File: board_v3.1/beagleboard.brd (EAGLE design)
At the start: 69.8 x 54.6 mm, 32 parts, among them U1 DWM1000

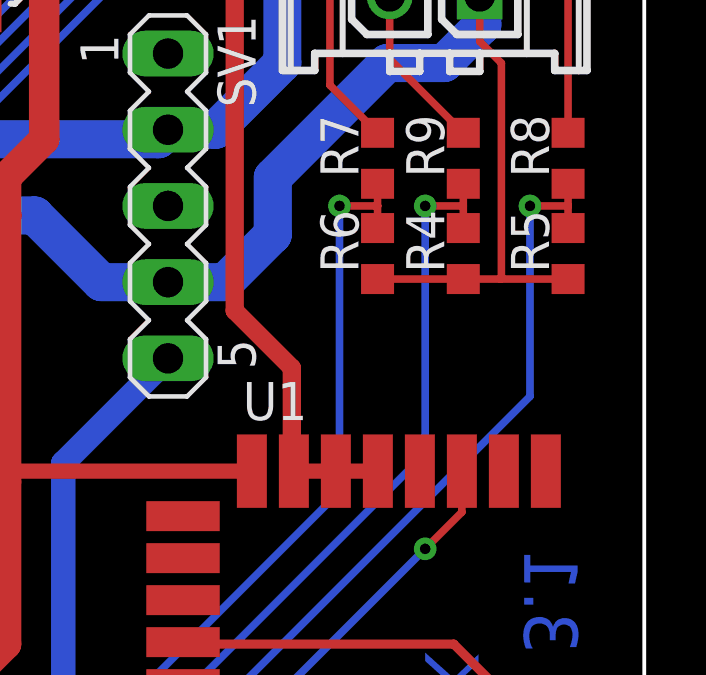
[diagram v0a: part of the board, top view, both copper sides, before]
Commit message: board v3.1 beta 6: poprawione acid-trap przy dzielnikach napięcia baterii
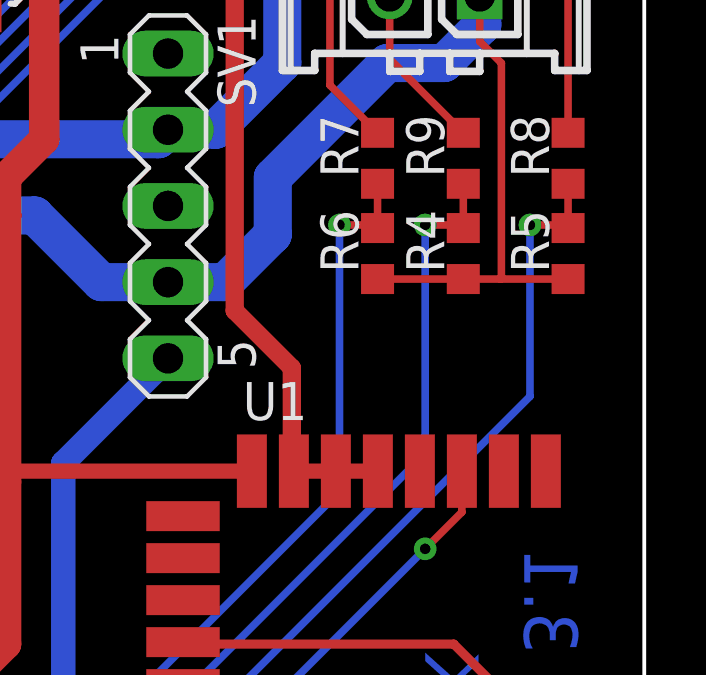
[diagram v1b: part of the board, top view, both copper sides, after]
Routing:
- net BAT_CELL3: track 41.6 -> 40.9 mm
- net BAT_CELL1: track 39.1 -> 38.5 mm
- net BAT_CELL2: track 39.5 -> 38.9 mm
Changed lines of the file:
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@@
 <contactref element="R8" pad="1"/>
 <contactref element="U$1" pad="86"/>
-<wire x1="68.58" y1="35.56" x2="69.85" y2="35.56" width="0.254" layer="1"/>
-<via x="68.58" y="35.56" extent="1-16" drill="0.35"/>
-<wire x1="68.58" y1="35.56" x2="68.58" y2="29.21" width="0.254" layer="16"/>
+<via x="68.58" y="34.925" extent="1-16" drill="0.35"/>
+<wire x1="68.58" y1="34.925" x2="68.58" y2="29.21" width="0.254" layer="16"/>
 <wire x1="68.58" y1="29.21" x2="53.34" y2="13.97" width="0.254" layer="16"/>
 <wire x1="53.34" y1="13.97" x2="53.34" y2="5.08" width="0.254" layer="16"/>
-<wire x1="69.85" y1="36.2975" x2="69.85" y2="35.56" width="0.254" layer="1"/>
-<wire x1="69.85" y1="35.56" x2="69.85" y2="34.8225" width="0.254" layer="1"/>
+<wire x1="69.85" y1="34.976153125" x2="69.85" y2="36.2975" width="0.254" layer="1"/>
+<wire x1="69.85" y1="34.976153125" x2="69.85" y2="34.8225" width="0.254" layer="1"/>
+<wire x1="68.58" y1="34.925" x2="69.798846875" y2="34.925" width="0.254" layer="1"/>
+<wire x1="69.798846875" y1="34.925" x2="69.85" y2="34.976153125" width="0.254" layer="1"/>
 </signal>
 <signal name="I2C2_SCL">
@@
 <contactref element="R7" pad="1"/>
 <contactref element="U$1" pad="81"/>
-<wire x1="62.23" y1="35.56" x2="63.5" y2="35.56" width="0.254" layer="1"/>
-<via x="62.23" y="35.56" extent="1-16" drill="0.35"/>
+<via x="62.23" y="34.925" extent="1-16" drill="0.35"/>
 <wire x1="62.23" y1="26.035" x2="49.53" y2="13.335" width="0.254" layer="16"/>
 <wire x1="49.53" y1="13.335" x2="49.53" y2="3.81" width="0.254" layer="16"/>
 <wire x1="49.53" y1="3.81" x2="48.26" y2="2.54" width="0.254" layer="16"/>
-<wire x1="62.23" y1="35.56" x2="62.23" y2="26.035" width="0.254" layer="16"/>
-<wire x1="63.5" y1="36.2975" x2="63.5" y2="35.56" width="0.254" layer="1"/>
-<wire x1="63.5" y1="35.56" x2="63.5" y2="34.8225" width="0.254" layer="1"/>
+<wire x1="62.23" y1="34.925" x2="62.23" y2="26.035" width="0.254" layer="16"/>
+<wire x1="63.5" y1="34.9303625" x2="63.5" y2="36.2975" width="0.254" layer="1"/>
+<wire x1="63.5" y1="34.9303625" x2="63.5" y2="34.8225" width="0.254" layer="1"/>
+<wire x1="62.23" y1="34.925" x2="63.4946375" y2="34.925" width="0.254" layer="1"/>
+<wire x1="63.4946375" y1="34.925" x2="63.5" y2="34.9303625" width="0.254" layer="1"/>
 </signal>
 <signal name="BAT_CELL1">
@@
 <contactref element="R9" pad="1"/>
 <contactref element="U$1" pad="84"/>
-<wire x1="66.3575" y1="34.8225" x2="66.3575" y2="35.56" width="0.254" layer="1"/>
-<wire x1="66.3575" y1="35.56" x2="66.3575" y2="36.2975" width="0.254" layer="1"/>
-<wire x1="66.3575" y1="35.56" x2="65.0875" y2="35.56" width="0.254" layer="1"/>
-<via x="65.0875" y="35.56" extent="1-16" drill="0.35"/>
-<wire x1="65.0875" y1="35.56" x2="65.0875" y2="27.305" width="0.254" layer="16"/>
+<wire x1="66.3575" y1="34.893728125" x2="66.3575" y2="34.8225" width="0.254" layer="1"/>
+<wire x1="66.3575" y1="34.893728125" x2="66.3575" y2="36.2975" width="0.254" layer="1"/>
+<via x="65.0875" y="34.925" extent="1-16" drill="0.35"/>
+<wire x1="65.0875" y1="34.925" x2="65.0875" y2="27.305" width="0.254" layer="16"/>
 <wire x1="65.0875" y1="27.305" x2="50.8" y2="13.0175" width="0.254" layer="16"/>
 <wire x1="50.8" y1="13.0175" x2="50.8" y2="5.08" width="0.254" layer="16"/>
+<wire x1="65.0875" y1="34.925" x2="66.326228125" y2="34.925" width="0.254" layer="1"/>
+<wire x1="66.326228125" y1="34.925" x2="66.3575" y2="34.893728125" width="0.254" layer="1"/>
 </signal>
 <signal name="DWM_RES">

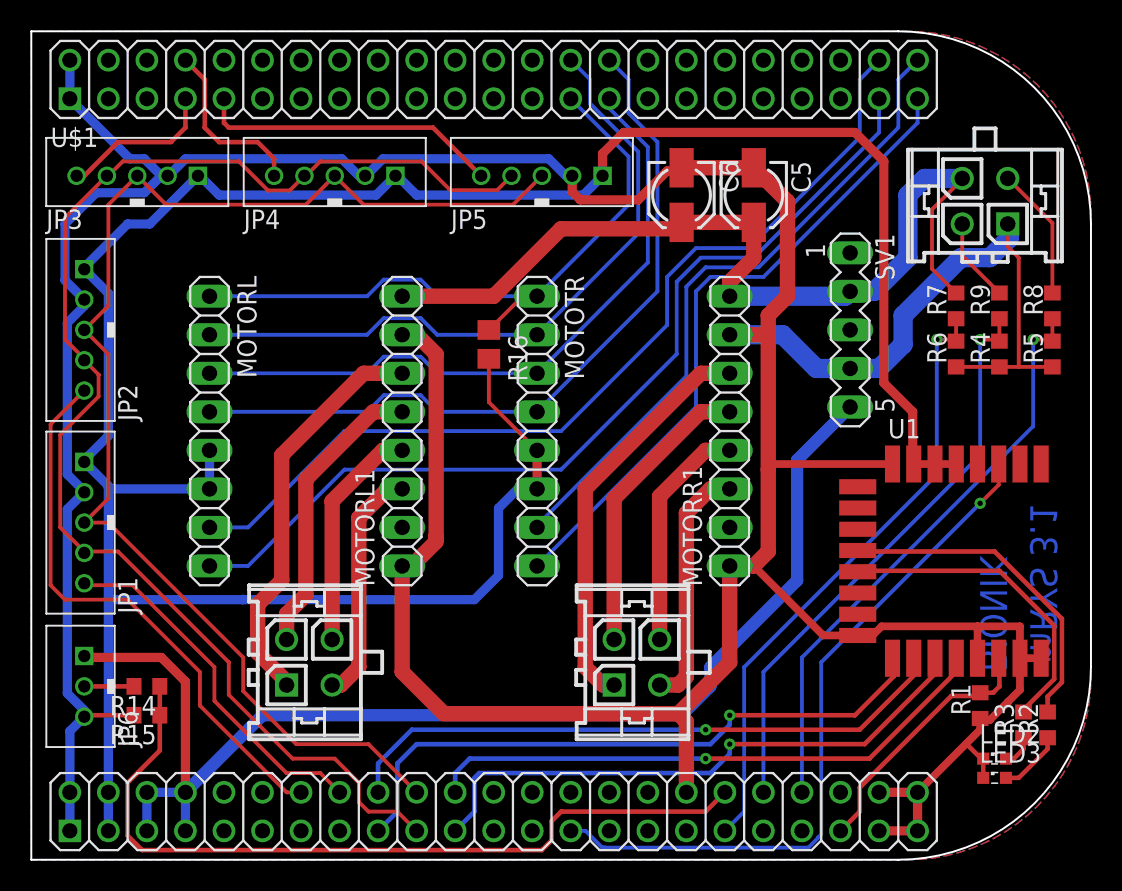
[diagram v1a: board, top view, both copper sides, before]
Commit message: board v3.1 beta 7: replaced DWM1000 module with connector for dwm1000-addon board, redone battery cell voltage routes. No more vias.
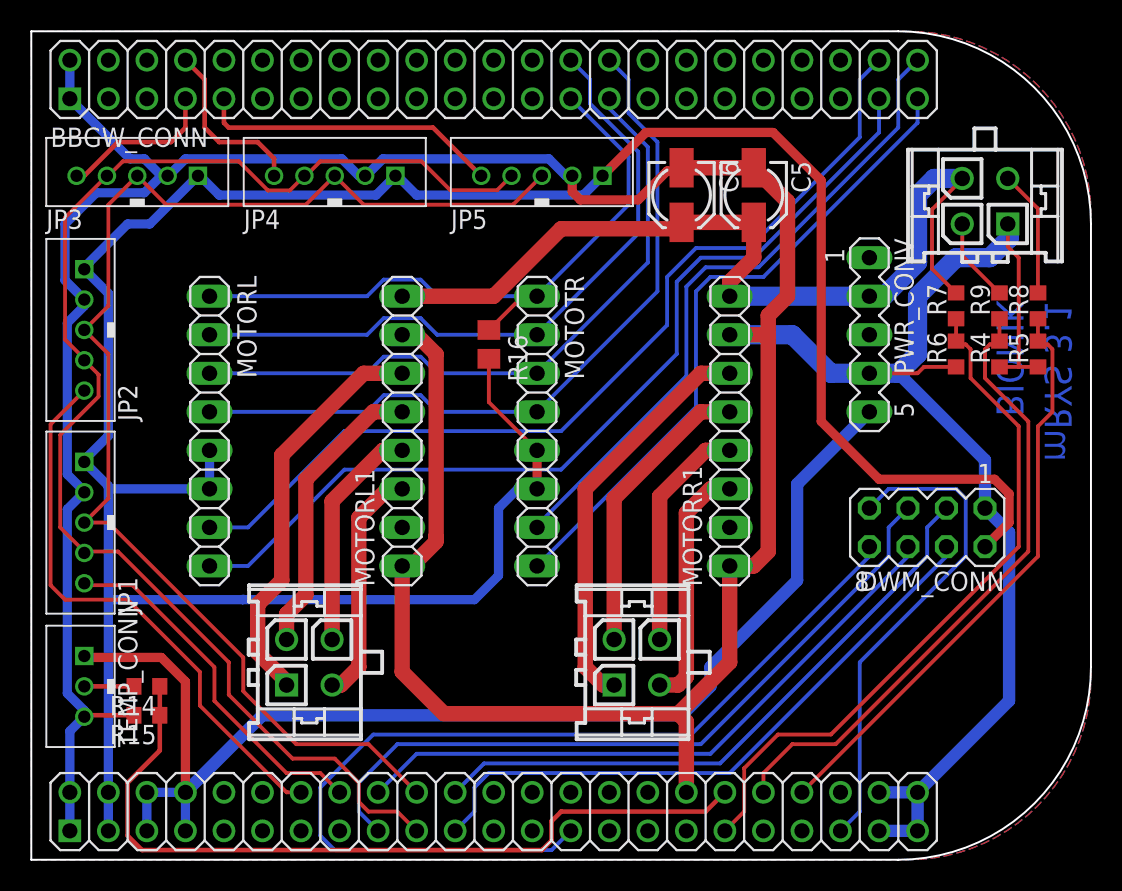
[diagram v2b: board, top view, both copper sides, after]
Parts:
- removed LED2, LED3: (no value), led:SML0603
- removed R1: 10k, rcl:R0603
- removed R2, R3: 330R, rcl:R0603
- removed SV1: (no value), con-lstb:MA05-1
- removed U1: DWM1000, DWM1000:XCVR_DWM1000
- added DWM_CONN: (no value), con-lstb:MA04-2
- added PWR_CONV: (no value), con-lstb:MA05-1
- moved R5 0.95 mm to (68.9, 34.0)
- moved R8 0.95 mm to (68.9, 37.1)
- renumbered JP6 to TEMP_CONN, MCONL to MOTORL_CONN, MCONR to MOTORR_CONN, U$1 to BBGW_CONN, X1 to BAT_CONN
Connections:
- removed net ENABLE: SV1.1
- removed net FL: MOTORL1.2
- removed net FR: MOTORR1.2
- removed net N$11: MOTORL1.3, MOTORL_CONN.P$3
- removed net N$15: MOTORR1.3, MOTORR_CONN.P$3
- removed net N$2: R3.2, U1.13
- removed net N$3: R2.2, U1.12
- removed net N$5: LED2.A, R3.1
- removed net N$6: LED3.A, R2.1
- net +12V: now also PWR_CONV.2; no longer SV1.2
- net +3V3: now also DWM_CONN.2; no longer U1.5, U1.6, U1.7
- net +5V: now also PWR_CONV.5; no longer SV1.5
- net DWM_IRQ: now also DWM_CONN.7; no longer R1.2, U1.22
- net DWM_RES: now also DWM_CONN.8; no longer U1.3
- net GND: now also DWM_CONN.1, PWR_CONV.4; no longer LED2.C, LED3.C, R1.1, SV1.4, U1.16, U1.21, U1.23, U1.24, U1.8
- net N$1: now also MOTORL1.3, MOTORL_CONN.P$3
- net N$14: now also MOTORR1.3, MOTORR_CONN.P$3
- net SPI0_CS0: now also DWM_CONN.5; no longer U1.17
- net SPI0_MISO: now also DWM_CONN.4; no longer U1.19
- net SPI0_MOSI: now also DWM_CONN.6; no longer U1.18
- net SPI0_SCLK: now also DWM_CONN.3; no longer U1.20
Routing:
- net N$3: track 21.9 -> 0.00 mm
- net N$2: track 21.0 -> 0.00 mm
- net DWM_RES: track 46.6 -> 63.7 mm, vias 1 -> 0
- net N$15: track 16.3 -> 0.00 mm
- net N$14: track 15.3 -> 31.6 mm
- net N$11: track 15.7 -> 0.00 mm
- net N$1: track 15.1 -> 30.9 mm
- net DWM_IRQ: track 17.2 -> 32.5 mm
- net GND: track 297.9 -> 285.9 mm
- net SPI0_CS0: track 41.7 -> 48.5 mm, vias 1 -> 0
- net +3V3: track 175.9 -> 182.2 mm
- net BAT_CELL3: track 40.9 -> 45.8 mm, vias 1 -> 0
- net N$6: track 4.27 -> 0.00 mm
- net BAT_CELL1: track 38.5 -> 41.9 mm, vias 1 -> 0
- net SPI0_SCLK: track 38.0 -> 41.3 mm, vias 1 -> 0
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
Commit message: board v3.1 beta 7: fixed bad networks between motor drivers and connectors; fixed some clearance issues
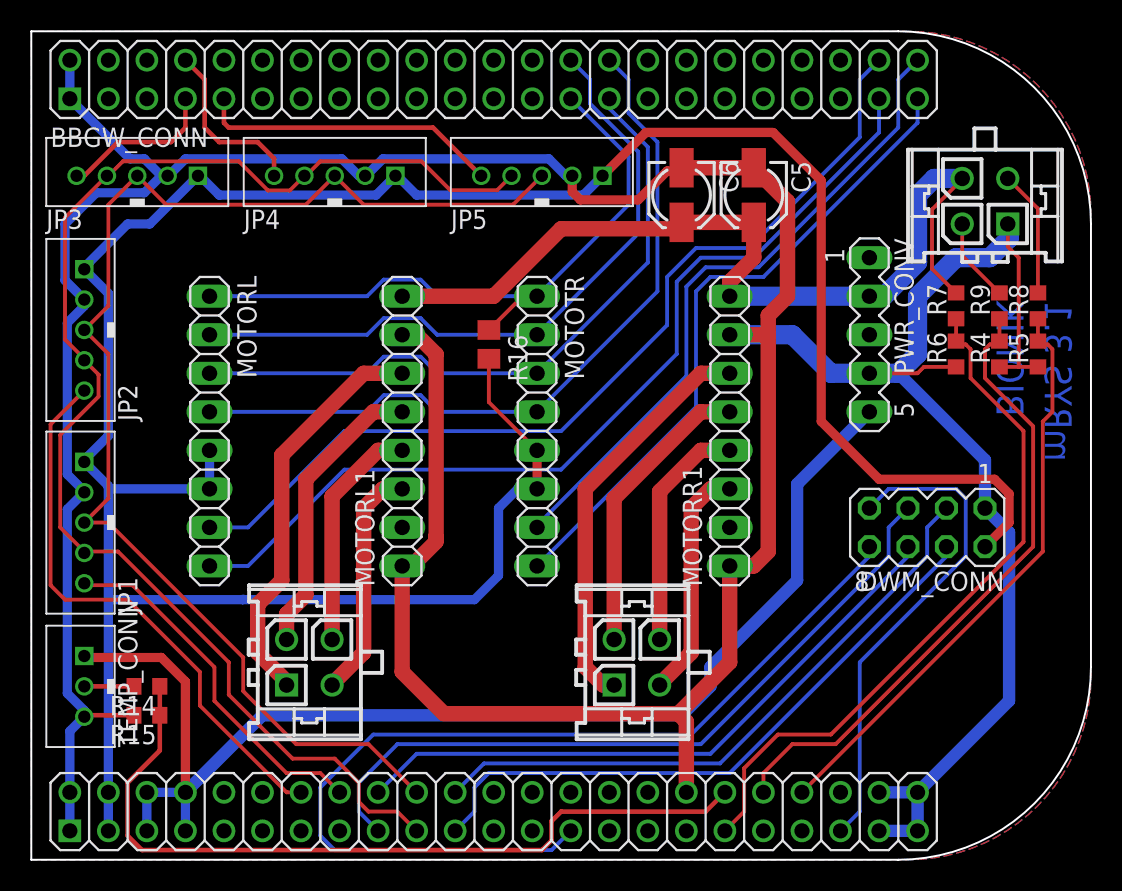
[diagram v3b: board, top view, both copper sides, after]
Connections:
- removed net N$14: MOTORR1.3, MOTORR1.4, MOTORR_CONN.P$3, MOTORR_CONN.P$4
- new net N$2: MOTORL1.4, MOTORL_CONN.P$4
- new net N$3: MOTORR1.3, MOTORR_CONN.P$3
- new net N$4: MOTORR1.4, MOTORR_CONN.P$4
- net N$1: no longer MOTORL1.4, MOTORL_CONN.P$4
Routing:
- net N$14: track 31.6 -> 0.00 mm
- net N$3: track 0.00 -> 15.6 mm
- net N$4: track 0.00 -> 15.5 mm
- net N$2: track 0.00 -> 15.3 mm
- net N$1: track 30.9 -> 15.6 mm
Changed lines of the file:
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@@
 <contactref element="BBGW_CONN" pad="86"/>
 <wire x1="68.8975" y1="34.8225" x2="68.8975" y2="36.2975" width="0.254" layer="1"/>
-<wire x1="53.34" y1="5.08" x2="68.8975" y2="20.6375" width="0.254" layer="1"/>
-<wire x1="68.8975" y1="20.6375" x2="68.8975" y2="29.21" width="0.254" layer="1"/>
-<wire x1="68.8975" y1="29.21" x2="69.85" y2="30.1625" width="0.254" layer="1"/>
+<wire x1="53.34" y1="5.08" x2="69.215" y2="20.955" width="0.254" layer="1"/>
+<wire x1="69.215" y1="20.955" x2="69.215" y2="29.5275" width="0.254" layer="1"/>
+<wire x1="69.215" y1="29.5275" x2="69.85" y2="30.1625" width="0.254" layer="1"/>
 <wire x1="69.85" y1="30.1625" x2="69.85" y2="34.29" width="0.254" layer="1"/>
 <wire x1="69.85" y1="34.29" x2="69.5325" y2="34.6075" width="0.254" layer="1"/>
@@
 <wire x1="25.0825" y1="30.1625" x2="26.9875" y2="30.1625" width="1.016" layer="1"/>
 </signal>
-<signal name="N$1">
-<contactref element="MOTORL1" pad="4"/>
-<contactref element="MOTORL_CONN" pad="P$4"/>
-<wire x1="22.3675" y1="15.1525" x2="22.3675" y2="24.2725" width="1.016" layer="1"/>
-<wire x1="22.3675" y1="24.2725" x2="25.7175" y2="27.6225" width="1.016" layer="1"/>
-<wire x1="25.7175" y1="27.6225" x2="26.9875" y2="27.6225" width="1.016" layer="1"/>
-<contactref element="MOTORL_CONN" pad="P$3"/>
-<contactref element="MOTORL1" pad="3"/>
-<wire x1="22.3675" y1="12.1525" x2="22.9475" y2="12.1525" width="1.016" layer="1"/>
-<wire x1="22.9475" y1="12.1525" x2="24.13" y2="13.335" width="1.016" layer="1"/>
-<wire x1="24.13" y1="13.335" x2="24.13" y2="23.1775" width="1.016" layer="1"/>
-<wire x1="24.13" y1="23.1775" x2="26.035" y2="25.0825" width="1.016" layer="1"/>
-<wire x1="26.035" y1="25.0825" x2="26.9875" y2="25.0825" width="1.016" layer="1"/>
-<wire x1="24.13" y1="23.1775" x2="22.3675" y2="24.2725" width="0" layer="19" extent="1-1"/>
-</signal>
 <signal name="N$12">
 <contactref element="MOTORR1" pad="6"/>
@@
 <wire x1="40.9575" y1="24.4475" x2="46.6725" y2="30.1625" width="1.016" layer="1"/>
 <wire x1="46.6725" y1="30.1625" x2="48.5775" y2="30.1625" width="1.016" layer="1"/>
-</signal>
-<signal name="N$14">
-<contactref element="MOTORR1" pad="4"/>
-<contactref element="MOTORR_CONN" pad="P$4"/>
-<wire x1="43.9575" y1="15.1525" x2="43.9575" y2="24.59" width="1.016" layer="1"/>
-<wire x1="43.9575" y1="24.59" x2="46.99" y2="27.6225" width="1.016" layer="1"/>
-<wire x1="46.99" y1="27.6225" x2="48.5775" y2="27.6225" width="1.016" layer="1"/>
-<contactref element="MOTORR_CONN" pad="P$3"/>
-<contactref element="MOTORR1" pad="3"/>
-<wire x1="43.9575" y1="12.1525" x2="45.1725" y2="12.1525" width="1.016" layer="1"/>
-<wire x1="45.1725" y1="12.1525" x2="45.72" y2="12.7" width="1.016" layer="1"/>
-<wire x1="45.72" y1="12.7" x2="45.72" y2="23.495" width="1.016" layer="1"/>
-<wire x1="45.72" y1="23.495" x2="47.3075" y2="25.0825" width="1.016" layer="1"/>
-<wire x1="47.3075" y1="25.0825" x2="48.5775" y2="25.0825" width="1.016" layer="1"/>
-<wire x1="45.72" y1="23.495" x2="43.9575" y2="24.59" width="0" layer="19" extent="1-1"/>
 </signal>
 <signal name="TEMPSENS">
@@
 <wire x1="49.53" y1="6.6675" x2="51.7525" y2="8.89" width="0.254" layer="1"/>
 <wire x1="51.7525" y1="8.89" x2="55.245" y2="8.89" width="0.254" layer="1"/>
-<wire x1="55.245" y1="8.89" x2="67.6275" y2="21.2725" width="0.254" layer="1"/>
-<wire x1="67.6275" y1="21.2725" x2="67.6275" y2="29.21" width="0.254" layer="1"/>
-<wire x1="67.6275" y1="29.21" x2="64.4525" y2="32.385" width="0.254" layer="1"/>
+<wire x1="55.245" y1="8.89" x2="67.945" y2="21.59" width="0.254" layer="1"/>
+<wire x1="67.945" y1="21.59" x2="67.945" y2="28.8925" width="0.254" layer="1"/>
+<wire x1="67.945" y1="28.8925" x2="64.4525" y2="32.385" width="0.254" layer="1"/>
 <wire x1="64.4525" y1="32.385" x2="64.4525" y2="34.29" width="0.254" layer="1"/>
 <wire x1="64.4525" y1="34.29" x2="64.135" y2="34.6075" width="0.254" layer="1"/>
@@
 <wire x1="50.8" y1="6.35" x2="52.705" y2="8.255" width="0.254" layer="1"/>
 <wire x1="52.705" y1="8.255" x2="55.5625" y2="8.255" width="0.254" layer="1"/>
-<wire x1="55.5625" y1="8.255" x2="68.2625" y2="20.955" width="0.254" layer="1"/>
-<wire x1="68.2625" y1="20.955" x2="68.2625" y2="29.5275" width="0.254" layer="1"/>
-<wire x1="68.2625" y1="29.5275" x2="65.405" y2="32.385" width="0.254" layer="1"/>
+<wire x1="55.5625" y1="8.255" x2="68.58" y2="21.2725" width="0.254" layer="1"/>
+<wire x1="68.58" y1="21.2725" x2="68.58" y2="29.21" width="0.254" layer="1"/>
+<wire x1="68.58" y1="29.21" x2="65.405" y2="32.385" width="0.254" layer="1"/>
 <wire x1="65.405" y1="32.385" x2="65.405" y2="34.29" width="0.254" layer="1"/>
 <wire x1="65.405" y1="34.29" x2="65.7225" y2="34.6075" width="0.254" layer="1"/>
@@
 <contactref element="BBGW_CONN" pad="85"/>
 </signal>
+<signal name="N$1">
+<contactref element="MOTORL1" pad="3"/>
+<contactref element="MOTORL_CONN" pad="P$3"/>
+<wire x1="22.3675" y1="12.1525" x2="22.3675" y2="12.2075" width="1.016" layer="1"/>
+<wire x1="24.4475" y1="14.2875" x2="24.4475" y2="23.8125" width="1.016" layer="1"/>
+<wire x1="24.4475" y1="23.8125" x2="25.7175" y2="25.0825" width="1.016" layer="1"/>
+<wire x1="25.7175" y1="25.0825" x2="26.9875" y2="25.0825" width="1.016" layer="1"/>
+<wire x1="22.3675" y1="12.2075" x2="24.4475" y2="14.2875" width="1.016" layer="1"/>
+</signal>
+<signal name="N$2">
+<contactref element="MOTORL_CONN" pad="P$4"/>
+<contactref element="MOTORL1" pad="4"/>
+<wire x1="22.3675" y1="15.1525" x2="22.3675" y2="24.59" width="1.016" layer="1"/>
+<wire x1="22.3675" y1="24.59" x2="25.4" y2="27.6225" width="1.016" layer="1"/>
+<wire x1="25.4" y1="27.6225" x2="26.9875" y2="27.6225" width="1.016" layer="1"/>
+</signal>
+<signal name="N$3">
+<contactref element="MOTORR1" pad="3"/>
+<contactref element="MOTORR_CONN" pad="P$3"/>
+<wire x1="43.9575" y1="12.1525" x2="43.9575" y2="12.2075" width="1.016" layer="1"/>
+<wire x1="43.9575" y1="12.2075" x2="46.0375" y2="14.2875" width="1.016" layer="1"/>
+<wire x1="46.0375" y1="14.2875" x2="46.0375" y2="23.8125" width="1.016" layer="1"/>
+<wire x1="46.0375" y1="23.8125" x2="47.3075" y2="25.0825" width="1.016" layer="1"/>
+<wire x1="47.3075" y1="25.0825" x2="48.5775" y2="25.0825" width="1.016" layer="1"/>
+</signal>
+<signal name="N$4">
+<contactref element="MOTORR_CONN" pad="P$4"/>
+<contactref element="MOTORR1" pad="4"/>
+<wire x1="43.9575" y1="15.1525" x2="43.9575" y2="24.9075" width="1.016" layer="1"/>
+<wire x1="43.9575" y1="24.9075" x2="46.6725" y2="27.6225" width="1.016" layer="1"/>
+<wire x1="46.6725" y1="27.6225" x2="48.5775" y2="27.6225" width="1.016" layer="1"/>
+</signal>
 </signals>
